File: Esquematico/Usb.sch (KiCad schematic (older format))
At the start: 1 part

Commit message: Foot prints
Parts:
- removed J?: Conn_USB, symbol Connector:Conn_01x04_Female
- added J1: Conn_01x05_Female, symbol Connector:Conn_01x05_Female
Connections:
- net 3V3: now also J1.1 (Pin_1)
- net GND: now also J1.4 (Pin_4)
- net Rx: now also J1.3 (Pin_3)
- net Tx: now also J1.2 (Pin_2)
- new net 5V: J1.5 (Pin_5)
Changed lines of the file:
@@
 $EndDescr
 $Comp
-L power:GND #PWR?
+L power:GND #PWR0101
 U 1 1 61A9BEBF
-P 5950 3700
-F 0 "#PWR?" H 5950 3450 50  0001 C CNN
-F 1 "GND" H 5955 3527 50  0000 C CNN
-F 2 "" H 5950 3700 50  0001 C CNN
-F 3 "" H 5950 3700 50  0001 C CNN
-	1    5950 3700
+P 5950 3800
+F 0 "#PWR0101" H 5950 3550 50  0001 C CNN
+F 1 "GND" H 5955 3627 50  0000 C CNN
+F 2 "" H 5950 3800 50  0001 C CNN
+F 3 "" H 5950 3800 50  0001 C CNN
+	1    5950 3800
 	1    0    0    -1
 $EndComp
 Wire Wire Line
-	6100 3650 5950 3650
+	6100 3550 5950 3550
 Wire Wire Line
-	5950 3650 5950 3700
-Text HLabel 5900 3550 0    50   Input ~ 0
+	5950 3550 5950 3800
+Text HLabel 5900 3350 0    50   Input ~ 0
 Tx
 Text HLabel 5900 3450 0    50   Input ~ 0
@@
 	5900 3450 6100 3450
 Wire Wire Line
-	5900 3550 6100 3550
+	5900 3350 6100 3350
+Text HLabel 5900 3250 0    50   Input ~ 0
+3V3
+Wire Wire Line
+	5900 3250 6100 3250
 $Comp
-L Connector:Conn_01x04_Female J?
-U 1 1 61B53722
+L Connector:Conn_01x05_Female J1
+U 1 1 61B942FE
 P 6300 3450
-F 0 "J?" H 6328 3426 50  0000 L CNN
-F 1 "Conn_USB" H 6328 3335 50  0000 L CNN
+F 0 "J1" H 6328 3476 50  0000 L CNN
+F 1 "Conn_01x05_Female" H 6328 3385 50  0000 L CNN
 F 2 "" H 6300 3450 50  0001 C CNN
 F 3 "~" H 6300 3450 50  0001 C CNN
@@
 	1    0    0    -1
 $EndComp
-Text HLabel 5900 3350 0    50   Input ~ 0
-3V3
+Text GLabel 5900 3650 0    50   Input ~ 0
+5V
 Wire Wire Line
-	5900 3350 6100 3350
+	6100 3650 5900 3650
 $EndSCHEMATC

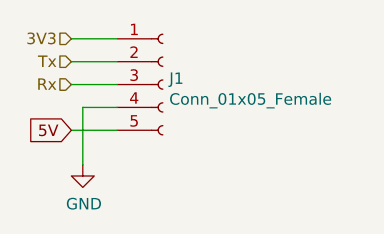
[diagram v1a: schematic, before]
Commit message: Carga elementos PCB
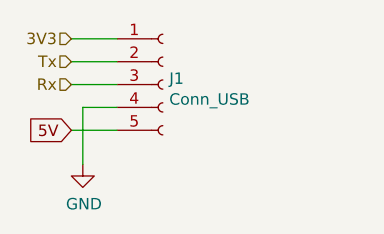
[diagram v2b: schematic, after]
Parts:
- J1: value Conn_01x05_Female -> Conn_USB; footprint (none) -> Connector_PinSocket_2.54mm:PinSocket_1x05_P2.54mm_Horizontal
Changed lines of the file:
@@
 P 6300 3450
 F 0 "J1" H 6328 3476 50  0000 L CNN
-F 1 "Conn_01x05_Female" H 6328 3385 50  0000 L CNN
-F 2 "" H 6300 3450 50  0001 C CNN
+F 1 "Conn_USB" H 6328 3385 50  0000 L CNN
+F 2 "Connector_PinSocket_2.54mm:PinSocket_1x05_P2.54mm_Horizontal" H 6300 3450 50  0001 C CNN
 F 3 "~" H 6300 3450 50  0001 C CNN
 	1    6300 3450
